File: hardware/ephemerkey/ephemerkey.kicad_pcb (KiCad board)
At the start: 2 copper layers, 62 parts, among them J1 SWD TC2030-NL, J2 LOCK IF (I2C JST-PH), J3 USB-C, J4 BAT 1S Li-ion, Q1 AO3401A, SW1 USER1, SW2 USER2, SW3 USER3/DFU, U1 STM32U083KCU6, U2 TPS63900DSKR, U3 USBLC6-2SC6, U4 MCP73831-2-OT, U5 LIS3DHTR, Y1 32.768kHz

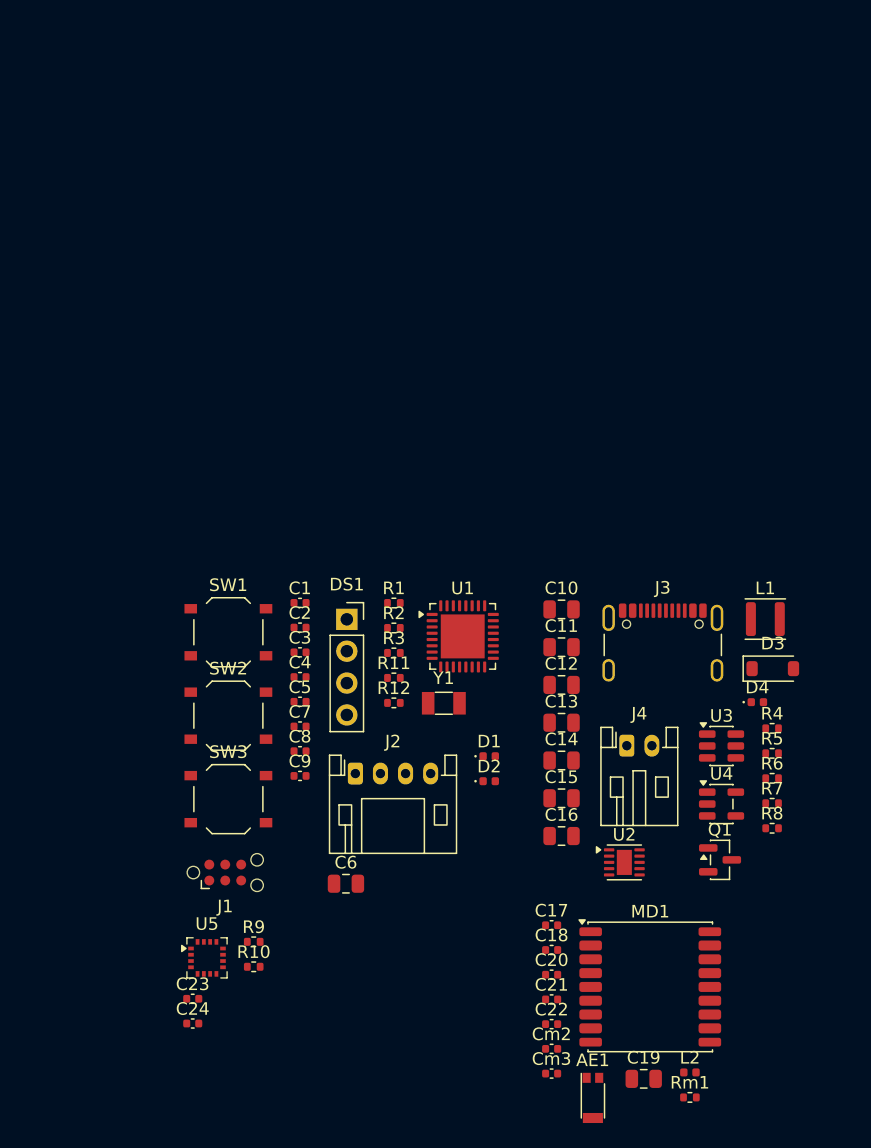
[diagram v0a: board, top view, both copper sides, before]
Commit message: ephemerkey: 2nd USB-C -> vertical GT-USB-7051A (C2843970), KiCad footprint
USB4085 was horizontal (GCT drawing: 'Dip Type, PCB Top Mount' -- cable inserts
parallel to the board), not the upright connector needed. Swap J5 to the
G-Switch GT-USB-7051A (C2843970): true vertical/upright SMT USB-C that sticks up
off the board, 16-pin USB2.0, ~3.5k JLCPCB stock, with a bundled KiCad footprint
(USB_C_Receptacle_G-Switch_GT-USB-7051x) + 3D model. Same symbol/bus as J3.

Co-Authored-By: Claude Opus 4.8 (1M context) <noreply@anthropic.com>
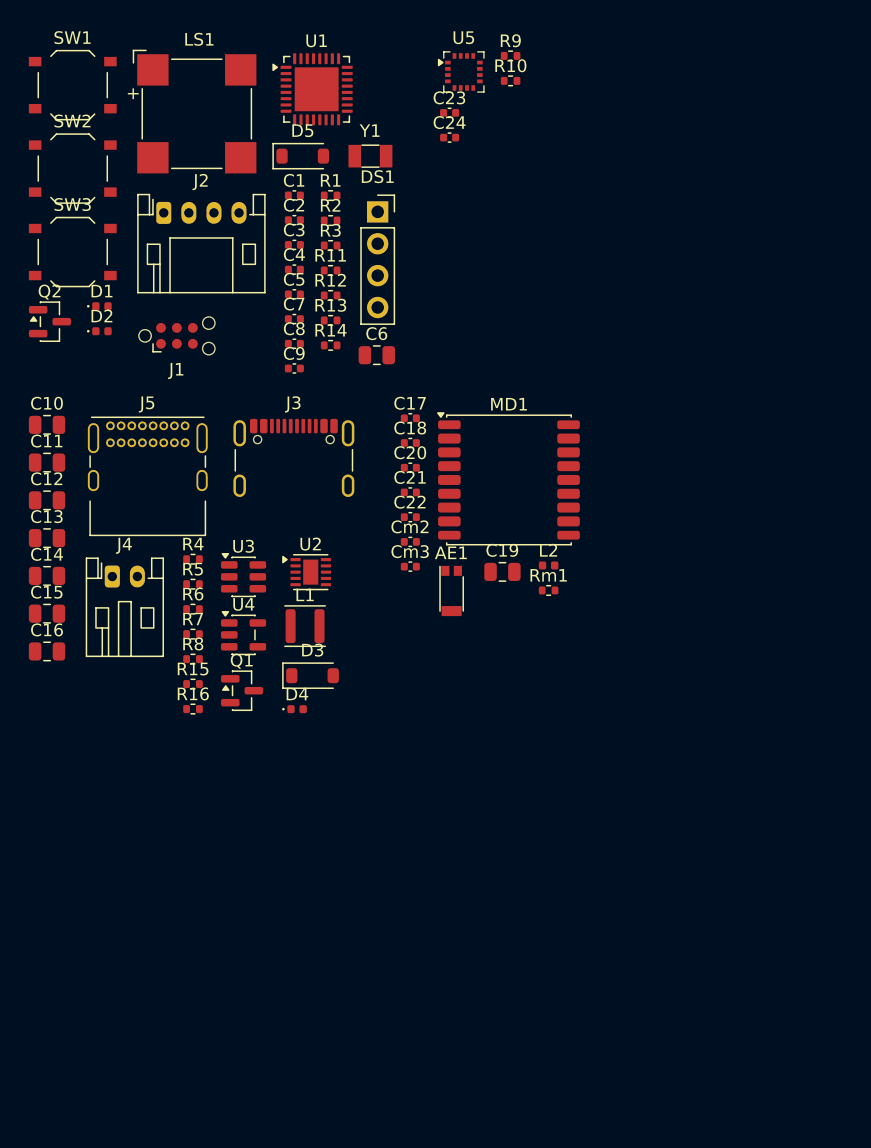
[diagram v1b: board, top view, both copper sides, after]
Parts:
- added D5: 1N4148W, Diode_SMD:D_SOD-123, F.Cu at (75.5, 42.9)
- added J5: USB-C (vert), Connector_USB:USB_C_Receptacle_GCT_USB4085, F.Cu at (60.2, 64.4)
- added LS1: MLT-8530, Buzzer_Beeper:MagneticBuzzer_CUI_CMT-8504-100-SMT, F.Cu at (67.1, 39.5)
- added Q2: AO3400A, Package_TO_SOT_SMD:SOT-23, F.Cu at (55.4, 56.1)
- added R13: 100R, Resistor_SMD:R_0402_1005Metric, F.Cu at (77.7, 56.0)
- added R14: 100k, Resistor_SMD:R_0402_1005Metric, F.Cu at (77.7, 58.0)
- added R15: 5.1k, Resistor_SMD:R_0402_1005Metric, F.Cu at (66.8, 85.0)
- added R16: 5.1k, Resistor_SMD:R_0402_1005Metric, F.Cu at (66.8, 86.9)
- Cm2: value DNP -> 1.8pF
- moved U5 73.5 mm to (88.3, 36.2)
- moved C23 73.5 mm to (87.2, 39.4)
- moved C24 73.5 mm to (87.2, 41.4)
- moved R10 73.5 mm to (92.1, 36.9)
- moved R9 73.5 mm to (92.1, 34.9)
- moved R4 48.1 mm to (66.8, 75.0)
- moved R6 48.1 mm to (66.8, 79.0)
- moved R7 48.1 mm to (66.8, 81.0)
- moved R5 48.1 mm to (66.8, 77.0)
- moved R8 48.1 mm to (66.8, 83.0)
- moved D1 47.3 mm to (59.5, 54.8)
- moved D2 47.3 mm to (59.5, 56.8)
- moved J2 47.2 mm to (64.4, 47.4)
- moved SW1 45.3 mm to (57.2, 37.2)
- moved SW3 45.3 mm to (57.2, 50.5)
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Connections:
- net GND renamed Net-(MD1-GND-Pad1)

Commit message: ephemerkey: vendor 3D model for the vertical USB-C (GT-USB-7051A)
The KiCad footprint for GT-USB-7051x references a STEP that's absent from this
(partial) 3D-model install. Fetched the model for C2843970 via easyeda2kicad
(EasyEDA/LCSC) -> lib/3dmodels/USB_C_GT-USB-7051A.step (2.3MB STEP), and added a
project footprint copy ephemerkey:USB_C_Receptacle_G-Switch_GT-USB-7051x with its
(model ...) repointed at the vendored file. J5 now uses the project footprint.
Verify model offset/rotation in the 3D viewer at layout (EasyEDA origin).

Co-Authored-By: Claude Opus 4.8 (1M context) <noreply@anthropic.com>
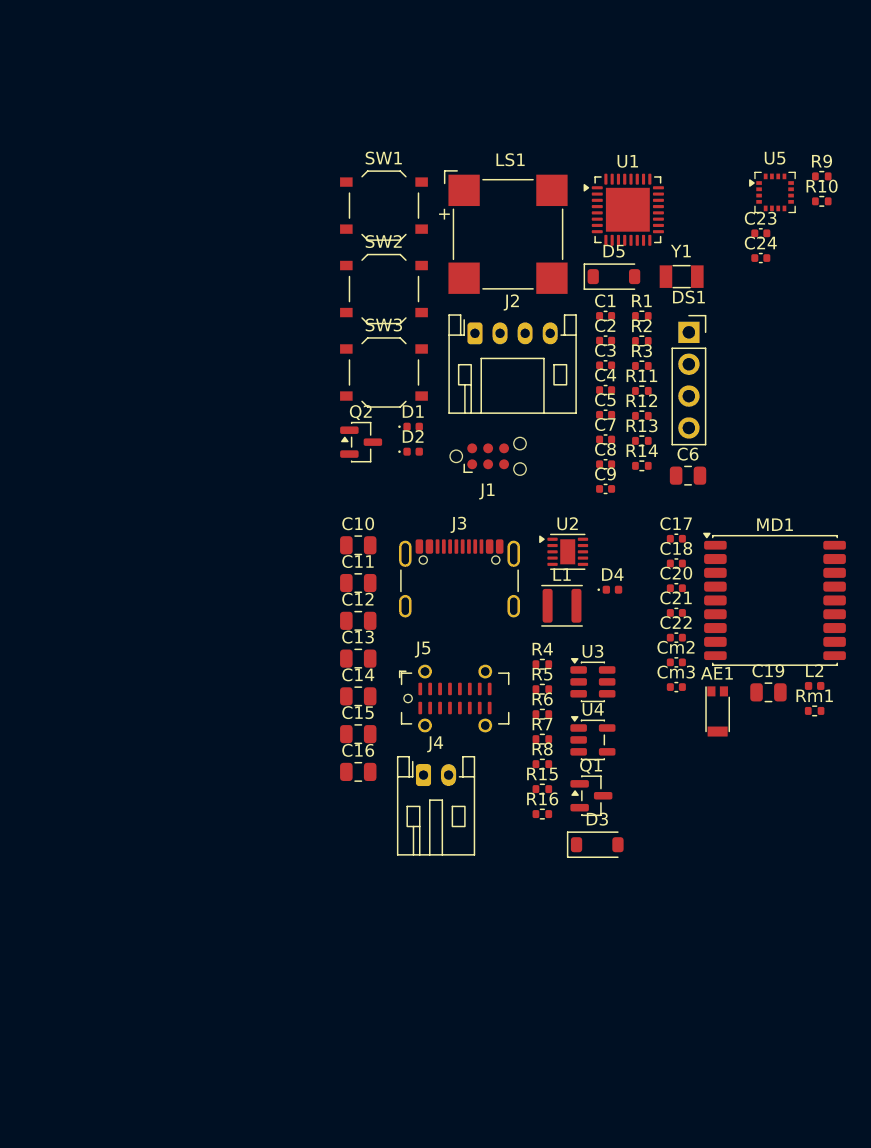
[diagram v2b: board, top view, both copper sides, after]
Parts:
- J5: footprint Connector_USB:USB_C_Receptacle_GCT_USB4085 -> Connector_USB:USB_C_Receptacle_G-Switch_GT-USB-7051x
- moved J5 35.0 mm to (87.6, 86.1)
- moved J4 29.4 mm to (85.1, 92.2)
- moved R15 29.1 mm to (94.6, 93.3)
- moved R16 29.1 mm to (94.6, 95.3)
- moved R4 29.1 mm to (94.6, 83.4)
- moved R6 29.1 mm to (94.6, 87.4)
- moved R7 29.1 mm to (94.6, 89.3)
- moved U3 29.1 mm to (98.6, 84.8)
- moved U4 29.1 mm to (98.6, 89.4)
- moved R5 29.1 mm to (94.6, 85.4)
- moved R8 29.1 mm to (94.6, 91.3)
- moved Q1 29.1 mm to (98.5, 93.9)
- moved D4 26.9 mm to (100.2, 77.4)
- moved J1 26.6 mm to (90.3, 66.8)
- moved C1 26.6 mm to (99.6, 55.6)
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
